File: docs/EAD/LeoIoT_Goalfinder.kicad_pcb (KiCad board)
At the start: 2 copper layers, 100 x 50 mm, 31 parts, among them J1 USB_B_Micro_Breakout, J2 LED Strip, J3 GAIN, Q1 IRFZ44N, U1 ESP32_D1_mini, U2 VL53L0X_Breakout, U3 MAX98357A_Breakout, U4 SW420_Breakout

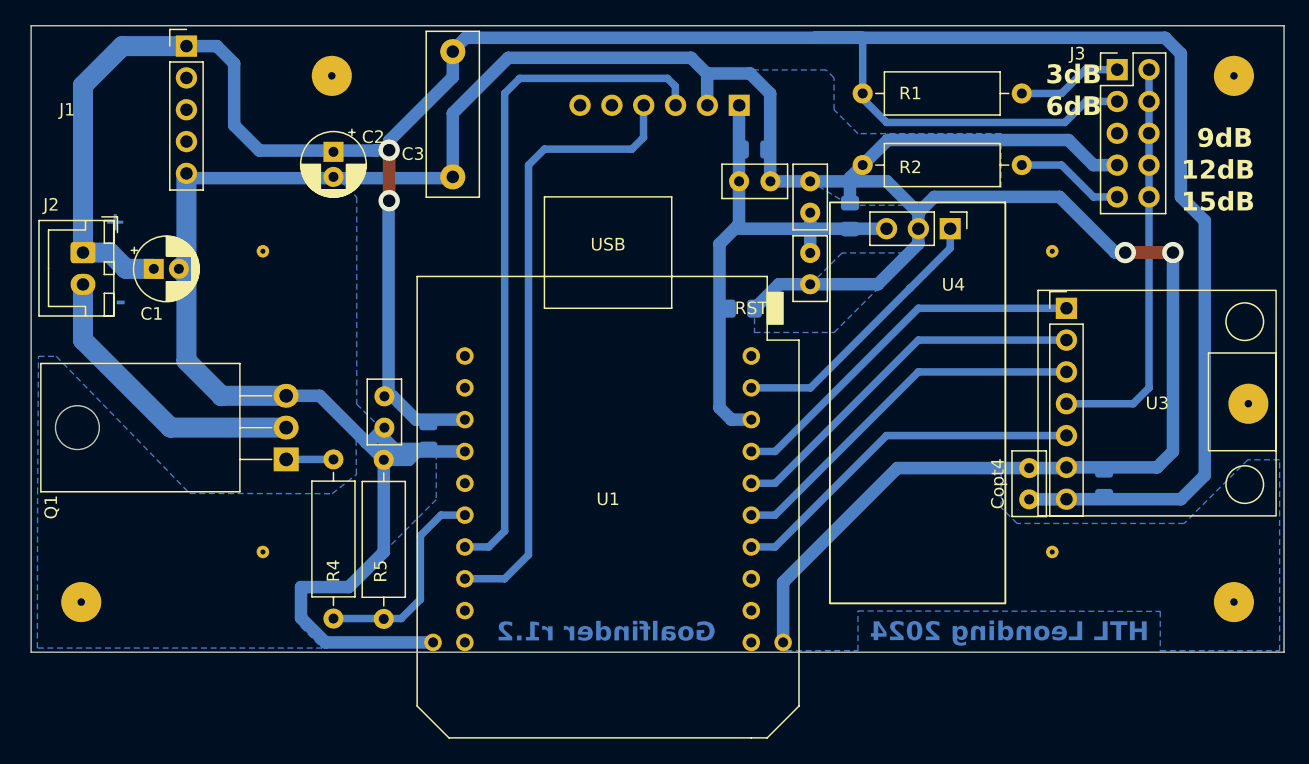
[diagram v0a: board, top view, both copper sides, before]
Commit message: Refined design and PCB layout and added BOM - added SMD resistors - shaped PCB prints
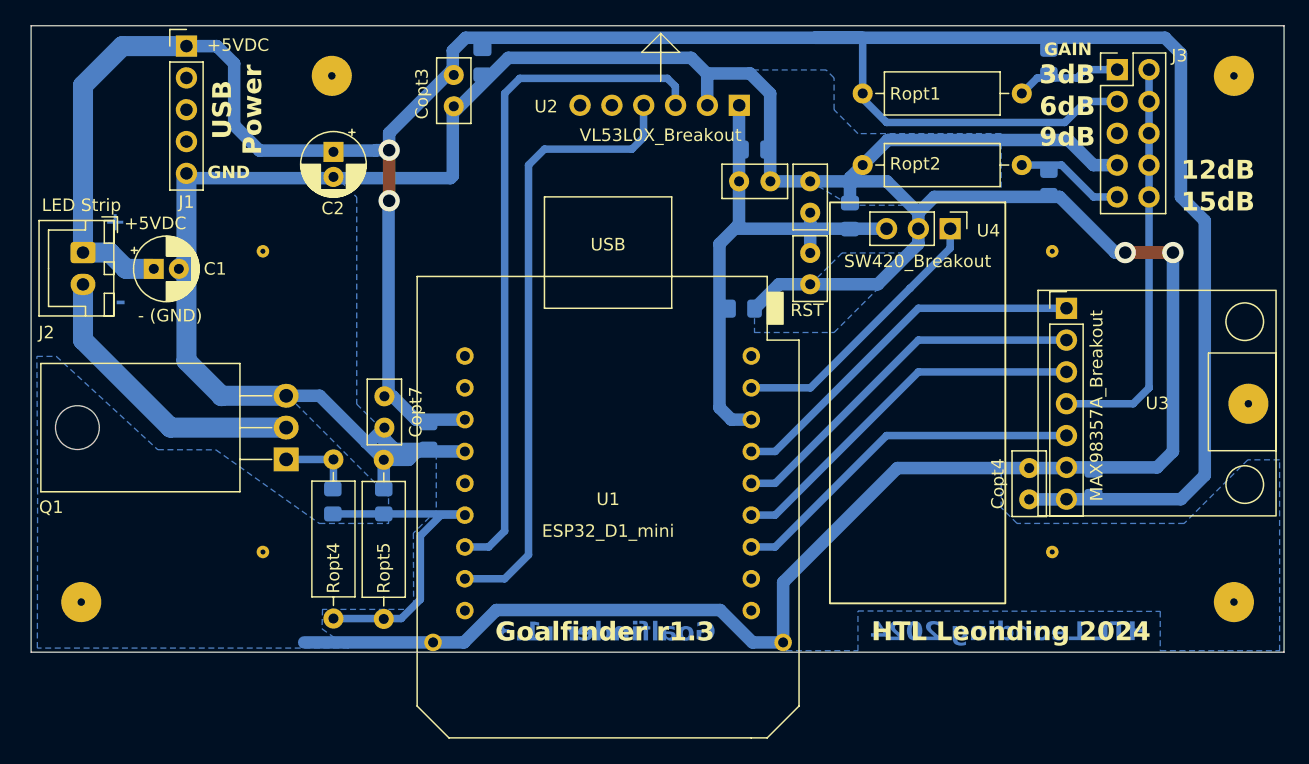
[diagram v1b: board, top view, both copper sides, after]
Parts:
- added Copt3: 100nF, Capacitor_THT:C_Disc_D5.0mm_W2.5mm_P2.50mm, F.Cu at (133.7, 63.9)
- added R1: 100k, Resistor_SMD:R_0805_2012Metric_Pad1.20x1.40mm_HandSolder, B.Cu at (181.2, 62.9)
- added R2: 100k, Resistor_SMD:R_0805_2012Metric_Pad1.20x1.40mm_HandSolder, B.Cu at (181.2, 72.5)
- added R4: 1k, Resistor_SMD:R_0805_2012Metric_Pad1.20x1.40mm_HandSolder, B.Cu at (124.1, 98.0)
- added R5: 33k, Resistor_SMD:R_0805_2012Metric_Pad1.20x1.40mm_HandSolder, B.Cu at (128.1, 98.0)
- C3: value 0,1µF -> 100nF; footprint Capacitor_THT:C_Rect_L13.0mm_W4.0mm_P10.00mm_FKS3_FKP3_MKS4 -> Capacitor_SMD:C_0805_2012Metric_Pad1.18x1.45mm_HandSolder; moved to B.Cu
- moved C3 2.50 mm to (136.0, 62.9)
- moved C4 0.85 mm to (184.8, 96.5)
- renumbered R1 to Ropt1, R2 to Ropt2, R4 to Ropt4, R5 to Ropt5
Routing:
- net GND: track 278.1 -> 291.6 mm
- net Net-(U1-IO_17/U2_TXC): track 16.9 -> 27.5 mm
- net Net-(Q1-G): track 3.77 -> 5.89 mm
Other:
- board text added: "+5VDC"
- board text added: "- (GND)"
- board text added: "GND"
- board text added: "Goalfinder r1.3"
- board text added: "USB Power"
- board text removed: "Goalfinder r1.2"

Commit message: added r1.4 of PCB and SMD-only PCB layout as well as production files
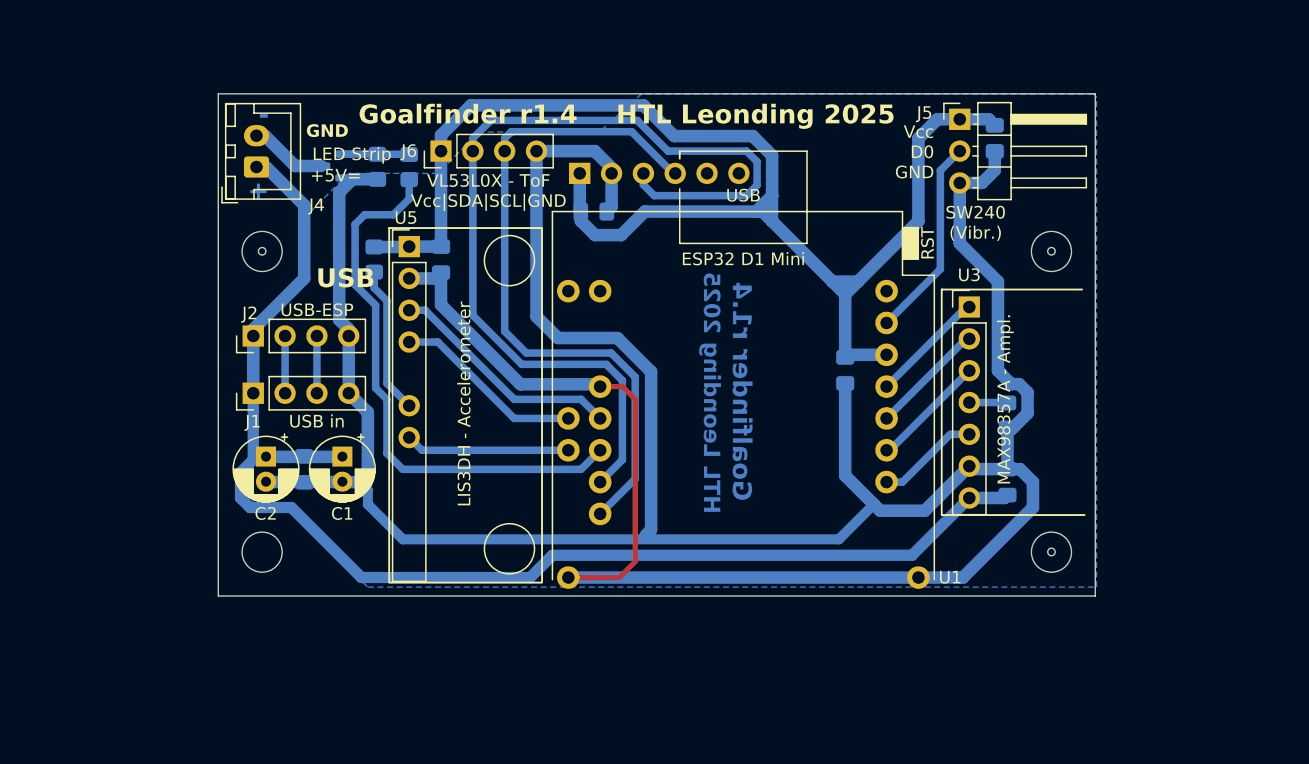
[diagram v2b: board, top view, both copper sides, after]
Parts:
- removed C7: 100nF, Capacitor_SMD:C_0805_2012Metric_Pad1.18x1.45mm_HandSolder
- removed Copt3, Copt4, Copt5, Copt6, Copt7, Copt8: 100nF, Capacitor_THT:C_Disc_D5.0mm_W2.5mm_P2.50mm
- removed J3: GAIN, Connector_PinHeader_2.54mm:PinHeader_2x05_P2.54mm_Vertical
- removed R1: 100k, Resistor_SMD:R_0805_2012Metric_Pad1.20x1.40mm_HandSolder
- removed REF**: MountingHole_3.2mm_M3, MountingHole:MountingHole_3.2mm_M3
- removed Ropt1, Ropt2: 100k, Resistor_THT:R_Axial_DIN0309_L9.0mm_D3.2mm_P12.70mm_Horizontal
- removed Ropt4: 1k, Resistor_THT:R_Axial_DIN0309_L9.0mm_D3.2mm_P12.70mm_Horizontal
- removed Ropt5: 33k, Resistor_THT:R_Axial_DIN0309_L9.0mm_D3.2mm_P12.70mm_Horizontal
- removed U4: SW420_Breakout, Breakout_Boards:SW420_Breakout_Board_Horizontal
- added C9: 100nF, Capacitor_SMD:C_0805_2012Metric_Pad1.18x1.45mm_HandSolder, B.Cu at (132.7, 78.7)
- added J2: USB-ESP, Connector_PinHeader_2.54mm:PinHeader_1x04_P2.54mm_Vertical, F.Cu at (117.7, 84.8)
- added J5: SW240 - Vcc/D0/GND, Connector_PinHeader_2.54mm:PinHeader_1x03_P2.54mm_Horizontal, F.Cu at (174.1, 67.5)
- added J6: VL53L0X-ToF Vcc/SDA/SCL/GND, Connector_PinHeader_2.54mm:PinHeader_1x04_P2.54mm_Vertical, F.Cu at (132.7, 70.0)
- added R3: 100k, Resistor_SMD:R_0805_2012Metric_Pad1.20x1.40mm_HandSolder, B.Cu at (127.4, 78.7)
- added U5: LIS3DH - Accelerometer, Breakout_Boards:LIS3DH_Breakout_Board, F.Cu at (128.6, 76.1)
- J1: value USB_B_Micro_Breakout -> USB in; footprint Breakout_Boards:Micro-USB_BreakoutBoard -> Connector_PinHeader_2.54mm:PinHeader_1x04_P2.54mm_Vertical
- J4: renamed from J2; footprint Connector_JST_2.54:JST_XH_B2B-XH-A_1x02_P2.54mm_Vertical -> Connector_JST:JST_XH_B2B-XH-A_1x02_P2.50mm_Vertical
- Q1: value IRFZ44N -> IRLML2502; footprint Package_TO_SOT_THT:TO-220-3_Horizontal_TabDown -> Package_TO_SOT_SMD:SOT-23; moved to B.Cu
- U1: value ESP32_D1_mini -> ESP32 D1 Mini
- U2: value VL53L0X_Breakout -> VL53L0X - ToF
- U3: value MAX98357A_Breakout -> MAX98357A - Ampl.
- moved C3 35.5 mm to (121.8, 95.4)
- moved J1 28.2 mm to (117.7, 89.3), turned to 90 degrees
- moved R4 27.4 mm to (130.2, 71.3)
- moved R5 26.7 mm to (127.6, 71.3), turned to -90 degrees
- moved C2 24.9 mm to (118.7, 94.4)
- moved Q1 23.7 mm to (124.1, 71.2), turned to 180 degrees
- moved C1 21.2 mm to (124.8, 94.4), turned to -90 degrees
- moved MH2 20.2 mm to (181.4, 78.0)
- moved R2 18.8 mm to (177.9, 91.1)
- moved J4 15.4 mm to (118.0, 71.3), turned to 90 degrees
- moved MH3 15.1 mm to (181.4, 102.0)
- moved MH1 15.1 mm to (118.4, 78.0)
- moved MH4 15.0 mm to (118.4, 102.0), turned to 0 degrees
- moved C6 13.8 mm to (144.9, 74.8)
- moved C5 13.1 mm to (176.9, 69.0), turned to -90 degrees
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- renumbered REF** to MH1, REF** to MH2, REF** to MH3, REF** to MH4
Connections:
- J1 pad 2: unconnected-(J1-D--Pad2) -> Net-(J1-Pin_2)
- J1 pad 3: unconnected-(J1-D+-Pad3) -> Net-(J1-Pin_3)
- J1 pad 4: unconnected-(J1-ID-Pad4) -> GND
- J4 pad 2: Net-(J2-Pin_2) -> /LED_PWR
- Q1 pad 2: Net-(J2-Pin_2) -> GND
- Q1 pad 3: GND -> /LED_PWR
- R2 pad 2: Net-(J3-Pad9) -> Net-(U3-GAIN_SLOT)
- R5 pad 1: Net-(U1-IO_17/U2_TXC) -> Net-(Q1-G)
- U1 pad 31: unconnected-(U1-IO_16/U2_RX-Pad31) -> Net-(U1-IO_16/U2_RX)
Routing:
- net 5V: track 227.1 -> 103.2 mm, vias 2 -> 0
- net 3V3: track 43.3 -> 111.4 mm
- net Net-(U3-GAIN_SLOT): track 32.5 -> 3.02 mm
- net Net-(J2-Pin_2): track 23.6 -> 0.00 mm
- net GND: track 291.6 -> 268.1 mm, vias 2 -> 0
- net Net-(U1-IO_19/MISO): track 29.9 -> 8.98 mm
- net Net-(U1-IO_05/SS): track 29.9 -> 8.98 mm
- net Net-(U1-IO_23/MOSI): track 29.9 -> 8.98 mm
- net Net-(U1-IO_18/CLK): track 28.8 -> 8.18 mm
- net Net-(J6-Pin_2): track 54.2 -> 74.3 mm
- net Net-(U1-IO_16/U2_RX): track 0.00 -> 18.8 mm
- net Net-(U1-IO_17/U2_TXC): track 27.5 -> 44.2 mm
- net Net-(U1-IO_04): track 0.00 -> 15.2 mm
- net Net-(U1-IO_12/TDI): track 0.00 -> 13.1 mm
- net Net-(U5-CS): track 0.00 -> 11.8 mm
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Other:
- board size 100 x 50 mm -> 70 x 40.1 mm
- board text added: "+5V="
- board text added: "ESP32-D1 internal"
- board text added: "Goalfinder r1.4"
- board text added: "HTL Leonding 2025"
- board text added: "R2: max. gain (15dB) --: med. gain ( 9dB)"
- board text added: "SW240 (Vibr.)"
- board text added: "USB"
- board text added: "VL53L0X - ToF Vcc|SDA|SCL|GND"
- board text added: "Vcc D0 GND"
- board text removed: "+5VDC"
- board text removed: "- (GND)"
- board text removed: "12dB"
- board text removed: "15dB"
- board text removed: "3dB"
- board text removed: "6dB"
- board text removed: "9dB"
- board text removed: "Goalfinder r1.3"
- board text removed: "HTL Leonding 2024"
- board text removed: "USB Power"

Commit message: finalized Goalfinder r1.4 + added optional accelerometer + added solder pads / pins for external USB socket and USB plug to ESP32 + added 'compact' variant with only SMD components + created production files for 'compact' variant + added images, renderings and models
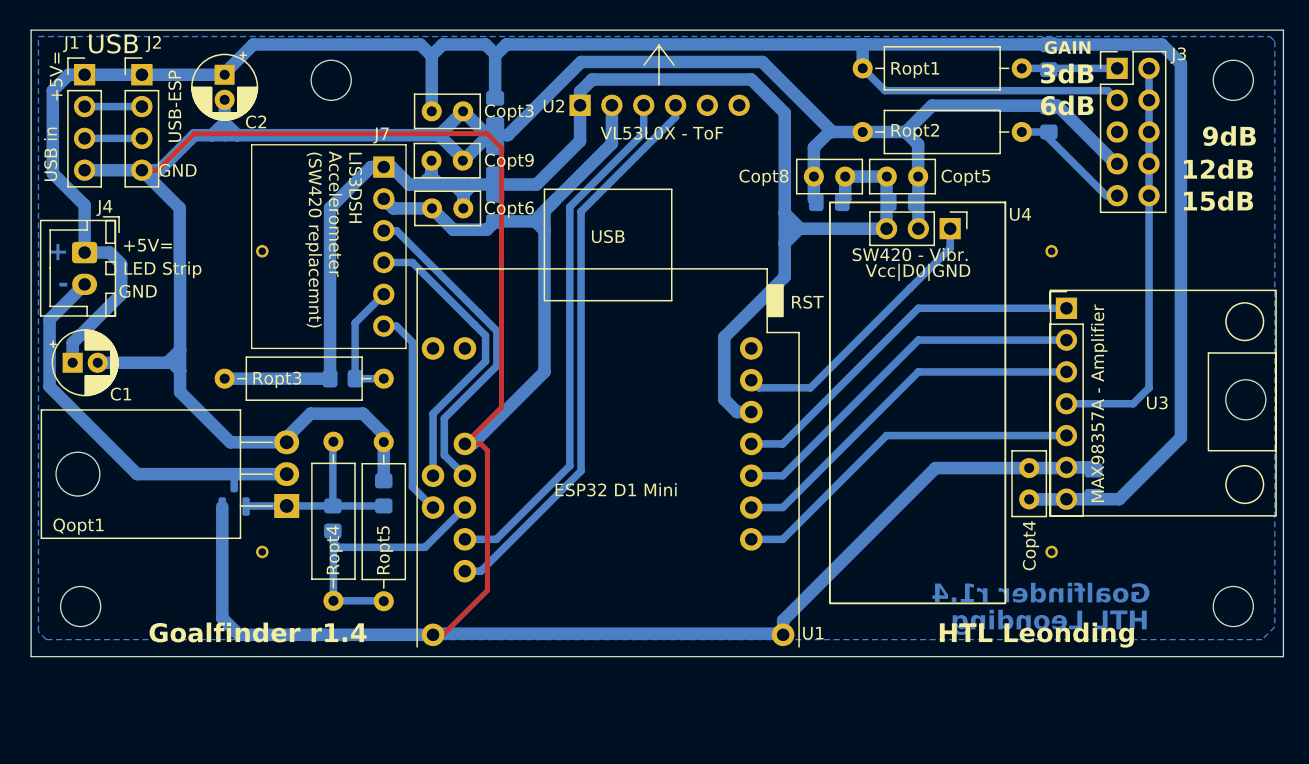
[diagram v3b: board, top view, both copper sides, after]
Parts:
- removed J5: SW240 - Vcc/D0/GND, Connector_PinHeader_2.54mm:PinHeader_1x03_P2.54mm_Horizontal
- removed J6: VL53L0X-ToF Vcc/SDA/SCL/GND, Connector_PinHeader_2.54mm:PinHeader_1x04_P2.54mm_Vertical
- removed the MH3 at (181.4, 102.0)
- removed U5: LIS3DH - Accelerometer, Breakout_Boards:LIS3DH_Breakout_Board
- added Copt3: 100nF, Capacitor_THT:C_Disc_D5.0mm_W2.5mm_P2.50mm, F.Cu at (132.0, 66.8)
- added Copt4: 100nF, Capacitor_THT:C_Disc_D5.0mm_W2.5mm_P2.50mm, F.Cu at (179.7, 97.8)
- added Copt5: 100nF, Capacitor_THT:C_Disc_D5.0mm_W2.5mm_P2.50mm, F.Cu at (168.3, 72.0)
- added Copt6: 100nF, Capacitor_THT:C_Disc_D5.0mm_W2.5mm_P2.50mm, F.Cu at (134.5, 74.6)
- added Copt8: 100nF, Capacitor_THT:C_Disc_D5.0mm_W2.5mm_P2.50mm, F.Cu at (165.0, 72.0)
- added Copt9: 100nF, Capacitor_THT:C_Disc_D5.0mm_W2.5mm_P2.50mm, F.Cu at (132.0, 70.8)
- added J3: GAIN, Connector_PinHeader_2.54mm:PinHeader_2x05_P2.54mm_Vertical, F.Cu at (186.7, 63.4)
- added J7: LIS3DH, Connector_PinHeader_2.54mm:PinHeader_1x06_P2.54mm_Horizontal, B.Cu at (128.1, 71.3)
- added MH3: MountingHole_3.2mm_M3, MountingHole:MountingHole_3.2mm_M3, F.Cu at (197.0, 89.9)
- added MH3: MountingHole_3.2mm_M3, MountingHole:MountingHole_3.2mm_M3, F.Cu at (196.0, 106.4)
- added Qopt1: IRLML2502, Package_TO_SOT_THT:TO-220-3_Horizontal_TabDown, F.Cu at (120.4, 98.3)
- added R1: 100k, Resistor_SMD:R_0805_2012Metric_Pad1.20x1.40mm_HandSolder, B.Cu at (181.2, 62.5)
- added Ropt1: 100k, Resistor_THT:R_Axial_DIN0309_L9.0mm_D3.2mm_P12.70mm_Horizontal, F.Cu at (166.4, 63.4)
- added Ropt2: 100k, Resistor_THT:R_Axial_DIN0309_L9.0mm_D3.2mm_P12.70mm_Horizontal, F.Cu at (166.4, 68.5)
- added Ropt3: 100k, Resistor_THT:R_Axial_DIN0309_L9.0mm_D3.2mm_P12.70mm_Horizontal, F.Cu at (115.4, 88.2)
- added Ropt4: 1k, Resistor_THT:R_Axial_DIN0309_L9.0mm_D3.2mm_P12.70mm_Horizontal, F.Cu at (124.1, 105.9)
- added Ropt5: 33k, Resistor_THT:R_Axial_DIN0309_L9.0mm_D3.2mm_P12.70mm_Horizontal, F.Cu at (128.1, 105.9)
- added U4: SW240 - Vcc/D0/GND, Breakout_Boards:SW420_Breakout_Board_Horizontal, F.Cu at (173.4, 76.2)
- J4: footprint Connector_JST:JST_XH_B2B-XH-A_1x02_P2.50mm_Vertical -> Connector_JST_2.54:JST_XH_B2B-XH-A_1x02_P2.54mm_Vertical
- U3: value MAX98357A - Ampl. -> MAX98357A - Amplifier
- moved C3 32.4 mm to (137.0, 66.8)
- moved C2 30.7 mm to (115.4, 63.9)
- moved J1 28.8 mm to (104.3, 63.9), turned to 0 degrees
- moved R4 28.7 mm to (124.1, 99.3)
- moved Q1 27.4 mm to (116.2, 97.4), turned to 90 degrees
- moved R5 26.1 mm to (128.1, 97.3), turned to 90 degrees
- moved R2 23.9 mm to (181.2, 67.5), turned to -90 degrees
- moved C1 22.8 mm to (103.3, 86.9), turned to 0 degrees
- moved J2 22.7 mm to (108.8, 63.9), turned to 0 degrees
- moved MH2 19.9 mm to (196.0, 64.4)
- moved J4 15.3 mm to (104.3, 78.1), turned to -90 degrees
- moved MH4 15.1 mm to (104.0, 106.4), turned to -90 degrees
- moved MH1 14.7 mm to (124.0, 64.4)
- moved C8 13.5 mm to (163.7, 74.1), turned to 180 degrees
- moved U1 11.7 mm to (146.1, 97.2)
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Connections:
- R2 pad 2: Net-(U3-GAIN_SLOT) -> Net-(J3-Pad9)
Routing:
- net GND: track 268.1 -> 378.1 mm
- net 5V: track 103.2 -> 194.8 mm
- net Net-(J6-Pin_2): track 74.3 -> 42.0 mm
- net Net-(U3-GAIN_SLOT): track 3.02 -> 32.6 mm
- net /LED_PWR: track 6.16 -> 31.1 mm
- net Net-(U1-IO_17/U2_TXC): track 44.2 -> 21.2 mm
- net Net-(U1-IO_19/MISO): track 8.98 -> 29.6 mm
- net Net-(U1-IO_05/SS): track 8.98 -> 29.6 mm
- net Net-(U1-IO_23/MOSI): track 8.98 -> 29.6 mm
- net Net-(U1-IO_18/CLK): track 8.18 -> 28.6 mm
- net 3V3: track 111.4 -> 126.5 mm
- net Net-(Q1-G): track 5.13 -> 16.1 mm
- net Net-(J6-Pin_3): track 54.6 -> 44.9 mm
- net Net-(J3-Pad9): track 0.00 -> 9.72 mm
- net Net-(J7-Pin_4): track 15.2 -> 23.5 mm
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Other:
- board size 70 x 40.1 mm -> 100 x 50 mm
- board text added: "12dB"
- board text added: "15dB"
- board text added: "3dB"
- board text added: "6dB"
- board text added: "9dB"
- board text added: "ESP internal!"
- board text added: "HTL Leonding"
- board text added: "J7"
- board text added: "LIS3DSH Accelerometer (SW420 replacemnt)"
- board text added: "Vcc|D0|GND"
- board text added: "via ESP USB!"
- board text removed: "ESP32-D1 internal"
- board text removed: "HTL Leonding 2025"
- board text removed: "R2: max. gain (15dB) --: med. gain ( 9dB)"
- board text removed: "SW240 (Vibr.)"
- board text removed: "VL53L0X - ToF Vcc|SDA|SCL|GND"
- board text removed: "Vcc D0 GND"
